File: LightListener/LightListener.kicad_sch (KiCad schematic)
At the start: 20 parts, among them Q1 Q_Photo_NPN, Q2 Q_Photo_NPN, U1 NJM4580

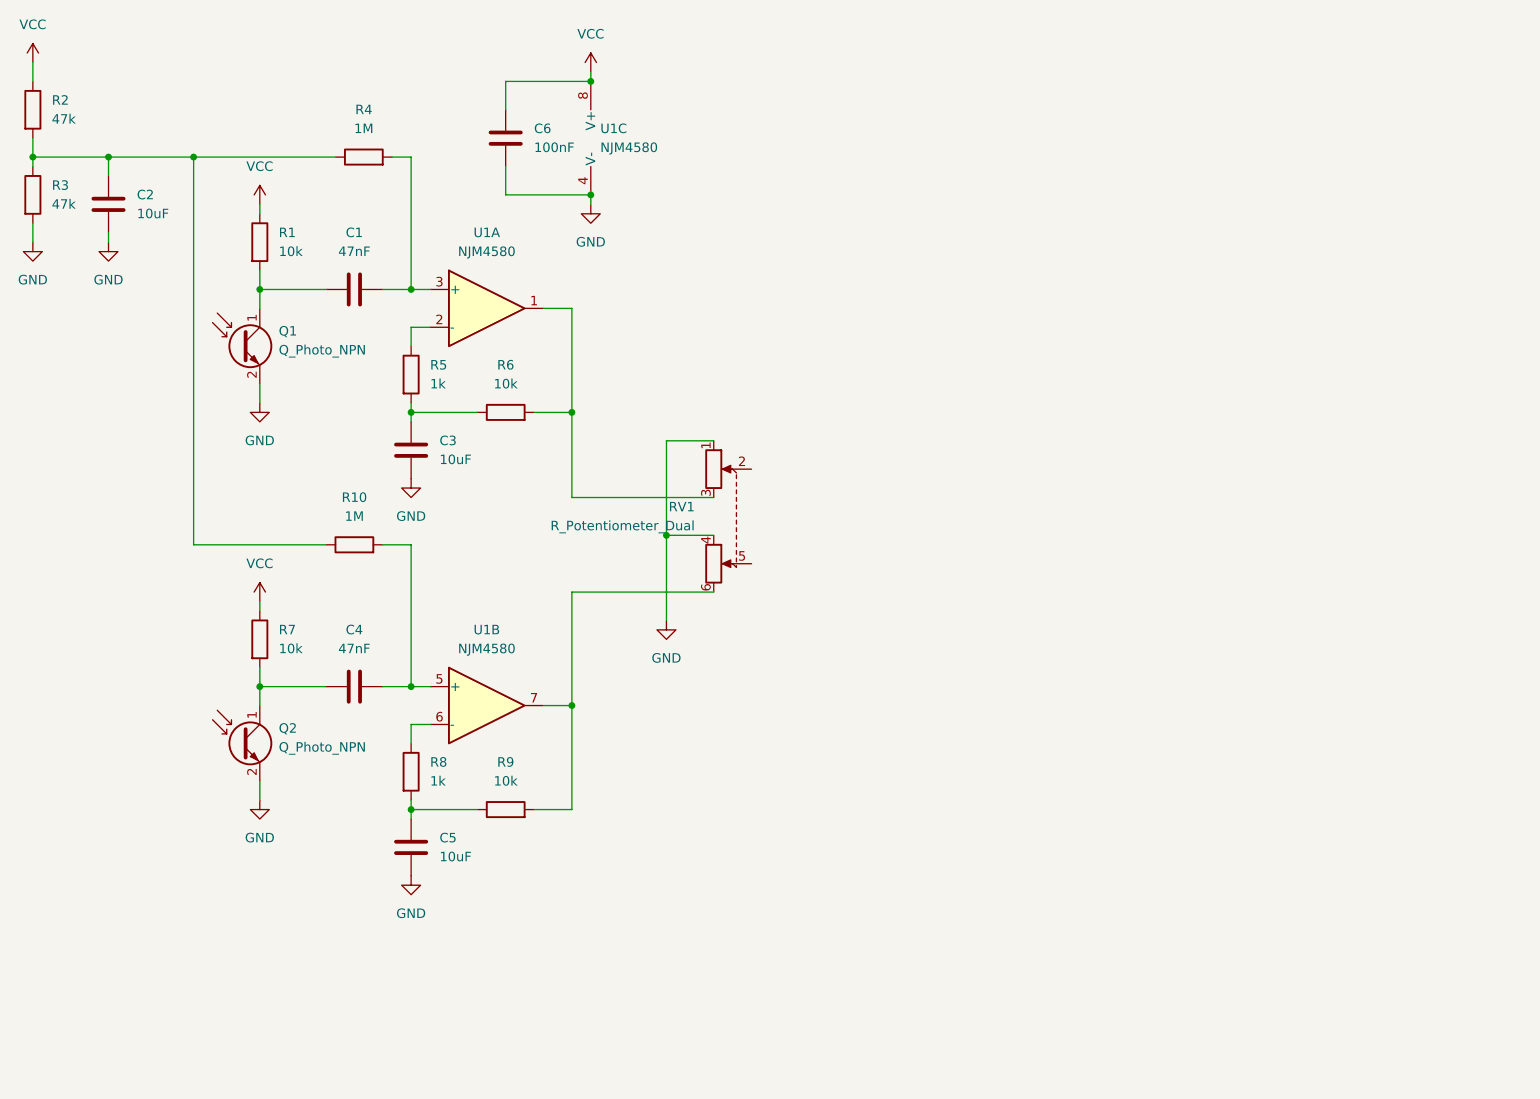
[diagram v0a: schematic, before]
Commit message: earphone amplifier
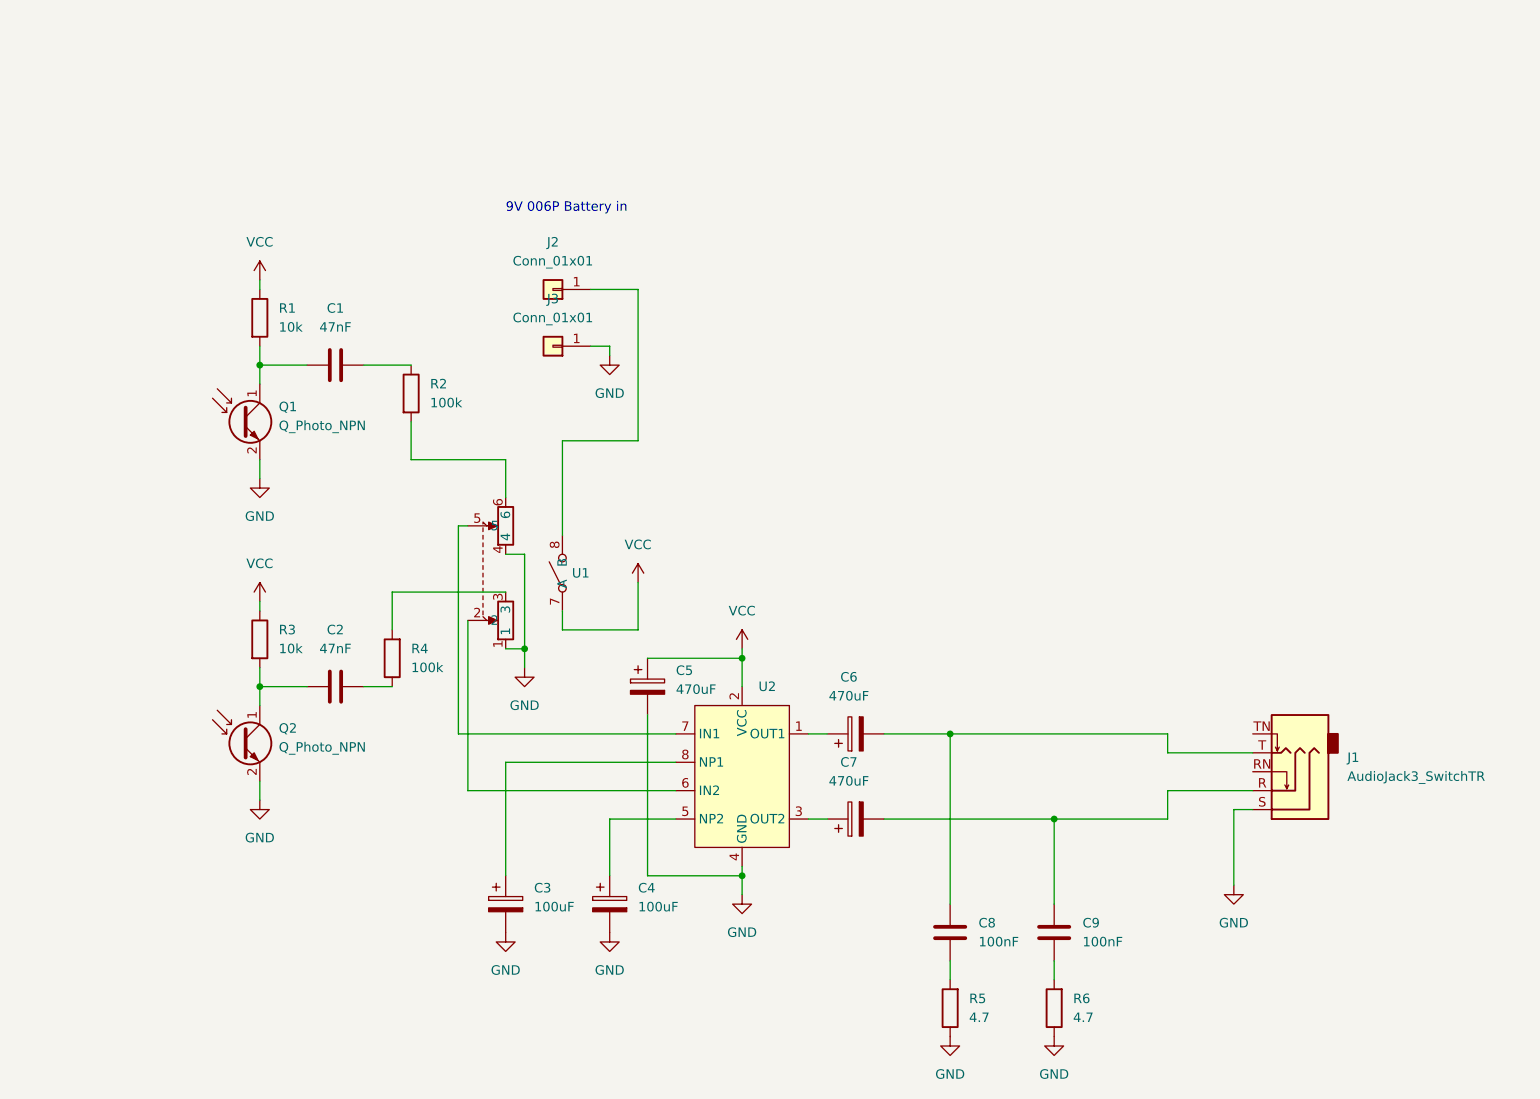
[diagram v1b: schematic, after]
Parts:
- removed C3, C5: 10uF, symbol Device:C
- removed C4: 47nF, symbol Device:C
- removed C6: 100nF, symbol Device:C
- removed R10: 1M, Resistor_SMD:R_0603_1608Metric, symbol Device:R
- removed R7, R9: 10k, Resistor_SMD:R_0603_1608Metric, symbol Device:R
- removed R8: 1k, Resistor_SMD:R_0603_1608Metric, symbol Device:R
- removed RV1: R_Potentiometer_Dual, Potentiometer_THT:Potentiometer_Alps_RK09L_Double_Horizontal, symbol Device:R_Potentiometer_Dual
- removed U1: NJM4580, symbol Amplifier_Operational:NJM4580
- added C3, C4: 100uF, symbol Device:C_Polarized
- added C5, C6, C7: 470uF, symbol Device:C_Polarized
- added C8, C9: 100nF, Capacitor_SMD:C_0603_1608Metric, symbol Device:C
- added J1: AudioJack3_SwitchTR, Loical_Library:MJ-495A, symbol Connector_Audio:AudioJack3_SwitchTR
- added J2, J3: Conn_01x01, symbol Connector_Generic:Conn_01x01
- added U1: ~, Potentiometer_THT:Potentiometer_Alps_RK097_Dual_Horizontal_Switch, symbol Local_Library:RK0972SA
- added U2: ~, Package_DIP:DIP-8_W7.62mm_LongPads, symbol Local_Library:TDA2822
- C1: footprint (none) -> Capacitor_SMD:C_0603_1608Metric
- C2: value 10uF -> 47nF; footprint (none) -> Capacitor_SMD:C_0603_1608Metric
- Q1, Q2: footprint (none) -> LED_THT:LED_D3.0mm_Horizontal_O1.27mm_Z2.0mm_IRBlack
- R2: value 47k -> 100k
- R3: value 47k -> 10k
- R4: value 1M -> 100k
- R5: value 1k -> 4.7
- R6: value 10k -> 4.7
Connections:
- net GND: now also R5.1, R6.1, C3.2, C4.2, C5.2, J1.S, J3.1 (Pin_1), U1.1, U1.4, U2.4 (GND); no longer C2.2, R3.2
- net VCC: now also R3.1, C5.1, U1.7 (A), U2.2 (VCC); no longer R2.1
- net at R6.2: now also C9.1
- net at R4.2: now also U1.3; no longer C1.2
- net at R5.2: now also C8.1; no longer R6.1
- net at Q2.1 (C): now also C2.1, R3.2
- new net: C3.1, U2.8 (NP1)
- new net: C6.2, C8.2, J1.T
- new net: C2.2, R4.1
- new net: J2.1 (Pin_1), U1.8 (B)
- new net: C7.2, C9.2, J1.R
- new net: C7.1, U2.3 (OUT2)
- new net: U1.2, U2.6 (IN2)
- new net: U1.5, U2.7 (IN1)
- new net: R2.2, U1.6
- new net: C6.1, U2.1 (OUT1)
- new net: C4.1, U2.5 (NP2)
- new net: C1.2, R2.1
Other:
- note added: "9V 006P Battery in"
- moved on the sheet: Q1, R1

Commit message: footprint assignment
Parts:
- removed C3, C4: 100uF, symbol Device:C_Polarized
- added C3, C4: 100uF, Capacitor_SMD:C_1206_3216Metric, symbol Device:C
- C5, C6, C7: footprint (none) -> Capacitor_SMD:CP_Elec_8x11.9
- J2, J3: footprint (none) -> Connector_Wire:SolderWirePad_1x01_SMD_5x10mm
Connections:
- net GND: now also C3.2, C4.2
- net at U2.8 (NP1): now also C3.1
- net at U2.5 (NP2): now also C4.1
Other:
- company: (none) -> Ponoor Experiments inc.
- title: (none) -> Stereo Light Receiver
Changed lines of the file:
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@@
 (kicad_sch (version 20230121) (generator eeschema)
   (paper "A4")
+  (title_block
+    (title "Stereo Light Receiver")
+    (date "2024-03-17")
+    (rev "0.1.0")
+    (company "Ponoor Experiments inc.")
+  )
   (junction (at 116.84 132.08) (diameter 0) (color 0 0 0 0)
   )
@@
     )
   )
-  (symbol (lib_id "Device:C_Polarized") (at 85.09 135.89 0) (unit 1)
-    (in_bom yes) (on_board yes) (dnp no) (fields_autoplaced)
-    (property "Reference" "C3" (at 88.9 133.731 0)
-      (effects (font (size 1.27 1.27)) (justify left))
-    )
-    (property "Value" "100uF" (at 88.9 136.271 0)
-      (effects (font (size 1.27 1.27)) (justify left))
-    )
-    (property "Footprint" "" (at 86.0552 139.7 0)
-      (effects (font (size 1.27 1.27)) hide)
-    )
-    (property "Datasheet" "~" (at 85.09 135.89 0)
-      (effects (font (size 1.27 1.27)) hide)
-    )
-    (pin "1")
-    (pin "2")
-    (instances
-      (project "LightListener"
-        (path "/ad39a340-bbfc-48e0-8c8a-e66de62c709c"
-          (reference "C3") (unit 1)
+  (symbol (lib_id "Device:C") (at 99.06 135.89 0) (unit 1)
+    (in_bom yes) (on_board yes) (dnp no) (fields_autoplaced)
+    (property "Reference" "C4" (at 102.87 134.62 0)
+      (effects (font (size 1.27 1.27)) (justify left))
+    )
+    (property "Value" "100uF" (at 102.87 137.16 0)
+      (effects (font (size 1.27 1.27)) (justify left))
+    )
+    (property "Footprint" "Capacitor_SMD:C_1206_3216Metric" (at 100.0252 139.7 0)
+      (effects (font (size 1.27 1.27)) hide)
+    )
+    (property "Datasheet" "~" (at 99.06 135.89 0)
+      (effects (font (size 1.27 1.27)) hide)
+    )
+    (pin "1")
+    (pin "2")
+    (instances
+      (project "LightListener"
+        (path "/ad39a340-bbfc-48e0-8c8a-e66de62c709c"
+          (reference "C4") (unit 1)
         )
       )
@@
       (effects (font (size 1.27 1.27)))
     )
-    (property "Footprint" "" (at 91.44 60.96 0)
+    (property "Footprint" "Connector_Wire:SolderWirePad_1x01_SMD_5x10mm" (at 91.44 60.96 0)
       (effects (font (size 1.27 1.27)) hide)
     )
@@
       (effects (font (size 1.27 1.27)))
     )
-    (property "Footprint" "" (at 91.44 53.34 0)
+    (property "Footprint" "Connector_Wire:SolderWirePad_1x01_SMD_5x10mm" (at 91.44 53.34 0)
       (effects (font (size 1.27 1.27)) hide)
     )
@@
       (effects (font (size 1.27 1.27)))
     )
-    (property "Footprint" "" (at 135.89 123.4948 0)
+    (property "Footprint" "Capacitor_SMD:CP_Elec_8x11.9" (at 135.89 123.4948 0)
       (effects (font (size 1.27 1.27)) hide)
     )
@@
       (effects (font (size 1.27 1.27)) (justify left))
     )
-    (property "Footprint" "" (at 105.1052 110.49 0)
+    (property "Footprint" "Capacitor_SMD:CP_Elec_8x11.9" (at 105.1052 110.49 0)
       (effects (font (size 1.27 1.27)) hide)
     )
@@
       (effects (font (size 1.27 1.27)))
     )
-    (property "Footprint" "" (at 135.89 112.0648 0)
+    (property "Footprint" "Capacitor_SMD:CP_Elec_8x11.9" (at 135.89 112.0648 0)
       (effects (font (size 1.27 1.27)) hide)
     )
@@
     )
   )
-  (symbol (lib_id "Device:C_Polarized") (at 99.06 135.89 0) (unit 1)
-    (in_bom yes) (on_board yes) (dnp no) (fields_autoplaced)
-    (property "Reference" "C4" (at 102.87 133.731 0)
-      (effects (font (size 1.27 1.27)) (justify left))
-    )
-    (property "Value" "100uF" (at 102.87 136.271 0)
-      (effects (font (size 1.27 1.27)) (justify left))
-    )
-    (property "Footprint" "" (at 100.0252 139.7 0)
-      (effects (font (size 1.27 1.27)) hide)
-    )
-    (property "Datasheet" "~" (at 99.06 135.89 0)
-      (effects (font (size 1.27 1.27)) hide)
-    )
-    (pin "1")
-    (pin "2")
-    (instances
-      (project "LightListener"
-        (path "/ad39a340-bbfc-48e0-8c8a-e66de62c709c"
-          (reference "C4") (unit 1)
-        )
-      )
-    )
-  )
   (symbol (lib_id "Device:Q_Photo_NPN") (at 49.53 71.12 0) (unit 1)
     (in_bom yes) (on_board yes) (dnp no) (fields_autoplaced)
@@
         )
       )
+    )
+  )
+  (symbol (lib_id "Device:C") (at 85.09 135.89 0) (unit 1)
+    (in_bom yes) (on_board yes) (dnp no) (fields_autoplaced)
+    (property "Reference" "C3" (at 88.9 134.62 0)
+      (effects (font (size 1.27 1.27)) (justify left))
+    )
+    (property "Value" "100uF" (at 88.9 137.16 0)
+      (effects (font (size 1.27 1.27)) (justify left))
+    )
+    (property "Footprint" "Capacitor_SMD:C_1206_3216Metric" (at 86.0552 139.7 0)
+      (effects (font (size 1.27 1.27)) hide)
+    )
+    (property "Datasheet" "~" (at 85.09 135.89 0)
+      (effects (font (size 1.27 1.27)) hide)
+    )
+    (pin "1")
+    (pin "2")
+    (instances
+      (project "LightListener"
+        (path "/ad39a340-bbfc-48e0-8c8a-e66de62c709c"
+          (reference "C3") (unit 1)
+        )
+      )
